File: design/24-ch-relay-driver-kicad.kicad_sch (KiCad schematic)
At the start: 6 parts

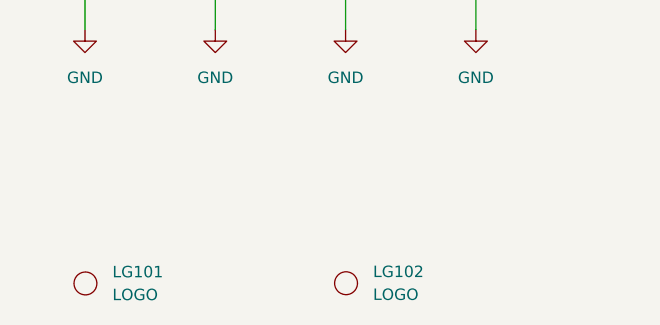
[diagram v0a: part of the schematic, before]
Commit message: Upgrade schematic to new KiCAD version.
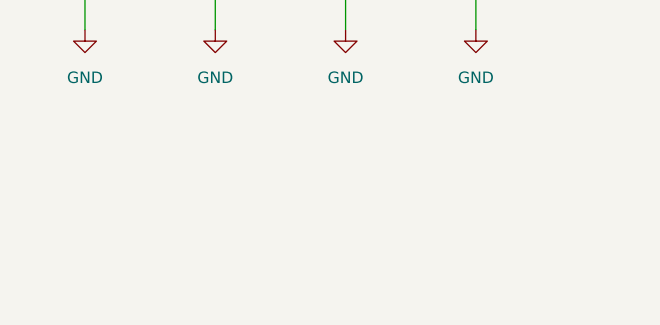
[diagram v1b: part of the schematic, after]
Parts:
- removed LG101: LOGO, simtelic:simtelic-5, symbol elect-generic-ic:LOGO
- removed LG102: LOGO, simtelic:simtelic-name-5, symbol elect-generic-ic:LOGO
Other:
- company: simtelic.com -> Dilshan R Jayakody
